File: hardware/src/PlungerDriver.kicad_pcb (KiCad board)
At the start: 2 copper layers, 80 x 16 mm, 35 parts, among them J1 MC 1,5/2, J2 locked, J3 S2B-PH, U1 16F1454, U2 TB67H450AFNG

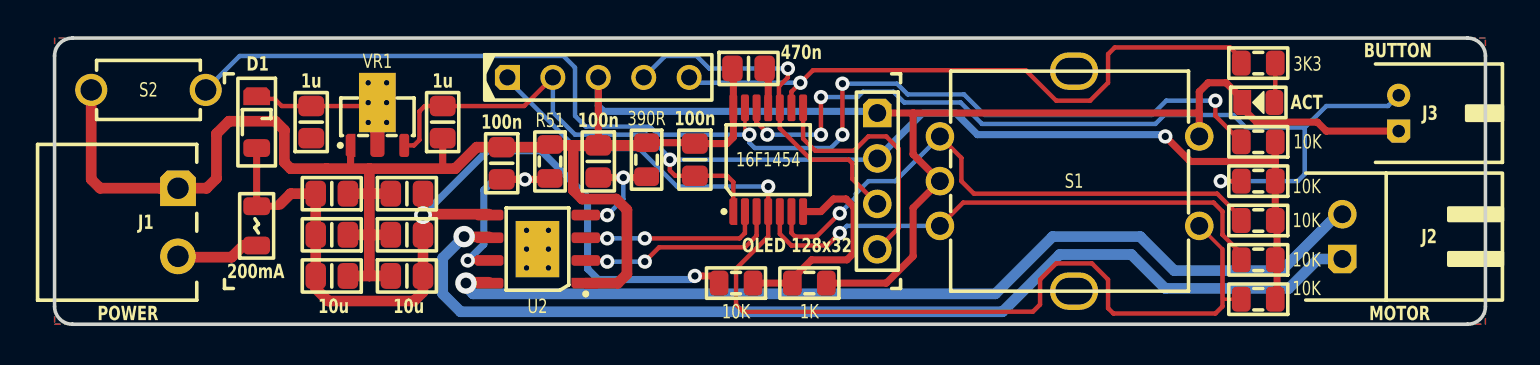
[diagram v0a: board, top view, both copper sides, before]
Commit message: Swapped I2C/SPI lines + general footprint update
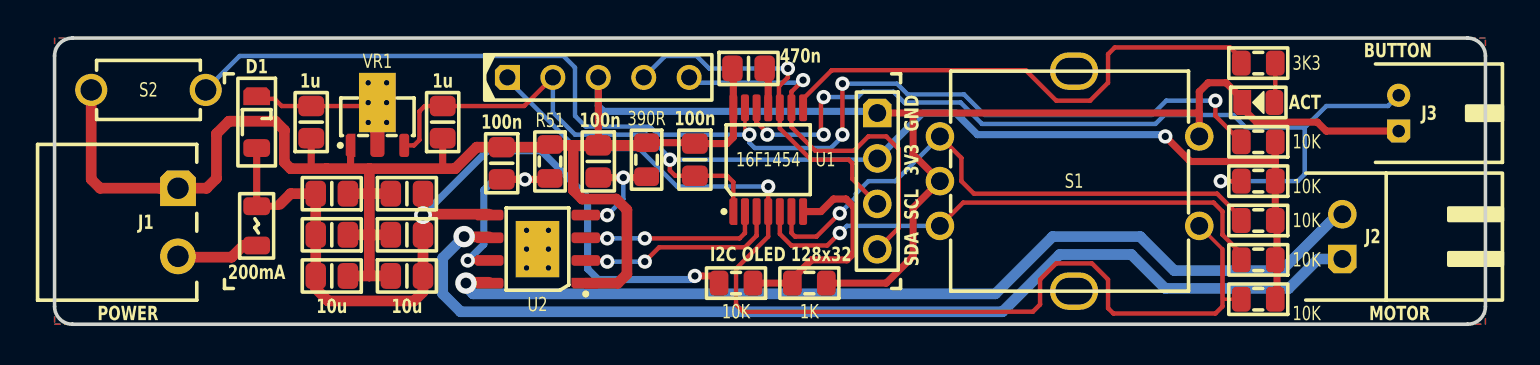
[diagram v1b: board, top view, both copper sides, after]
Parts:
- DS2: value OLED 128x32 -> I2C OLED 128x32
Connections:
- net OLED_SCK renamed OLED_SCL
- C5 pad 1: (no net) -> GND
- DS2 pad 4: OLED_SDO -> OLED_SDA
- ICSP pad 5: LED_ACT -> OLED_SDA
- U1 pad 8: OLED_SDO -> LED_ACT
- U1 pad 9: LED_ACT -> OLED_SDA
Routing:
- net OLED_SDA: track 0.00 -> 22.3 mm, vias 0 -> 1
- net OLED_SDO: track 14.1 -> 0.00 mm
- net LED_ACT: track 35.6 -> 28.8 mm, vias 1 -> 0
- net GND: track 153.6 -> 157.5 mm
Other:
- board text added: "3V3"
- board text added: "GND"
- board text added: "SCL"
- board text added: "SDA"

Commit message: Refactoring board a bit more
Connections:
- net Vdio renamed 5V
- net Vfused renamed 6V

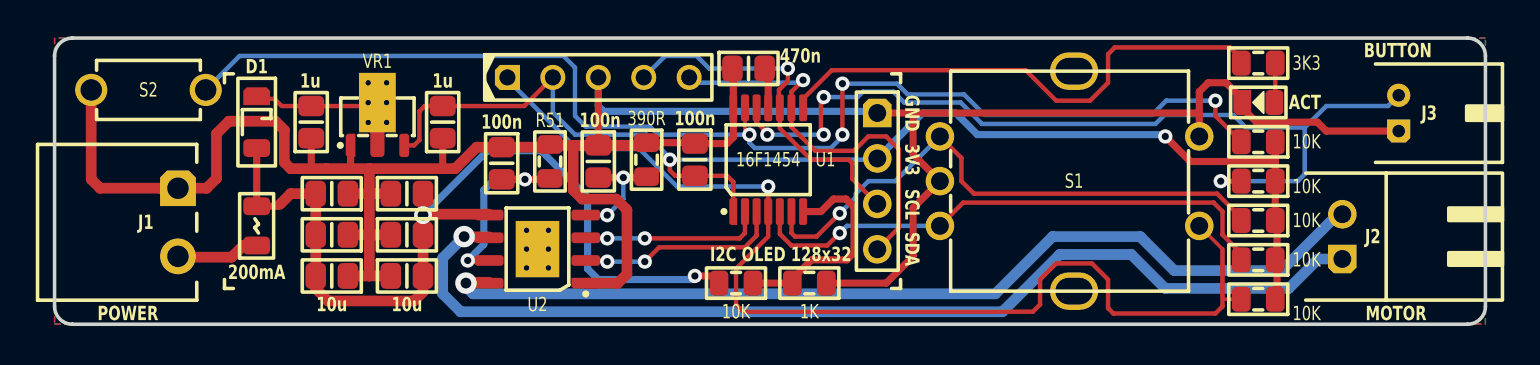
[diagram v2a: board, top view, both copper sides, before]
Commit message: Added I2C pullup resistors
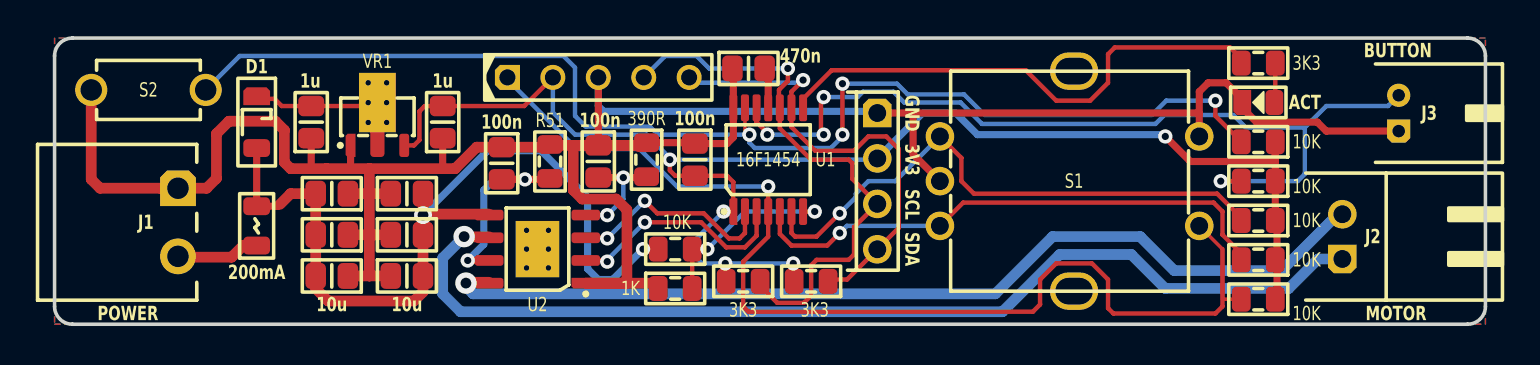
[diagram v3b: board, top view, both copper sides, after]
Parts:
- added R5: 3K3, Medo64:R (0805), F.Cu at (53.5, 28.6)
- added R6: 3K3, Medo64:R (0805), F.Cu at (57.3, 28.6)
- moved R3 7.51 mm to (49.7, 29.0), turned to 0 degrees
- moved R12 3.89 mm to (49.7, 26.8)
- renumbered R9 to R10, R10 to R11, R5 to R12, R6 to R7, R7 to R8, R8 to R9
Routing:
- net 3V3: track 72.2 -> 83.7 mm, vias 2 -> 5
- net OLED_SCL: track 20.0 -> 31.4 mm
- net GND: track 157.5 -> 151.7 mm
- net OLED_SDA: track 22.3 -> 25.8 mm
- net 6V: track 51.3 -> 48.6 mm
- net IN_ADC_INPUT_VOLTAGE: track 12.1 -> 10.4 mm, vias 0 -> 2
- net DRIVER_IN1: track 10.3 -> 12.0 mm
- net DRIVER_IN2: track 11.4 -> 12.7 mm
- net IN_ROTARY_SWITCH: track 65.0 -> 64.5 mm

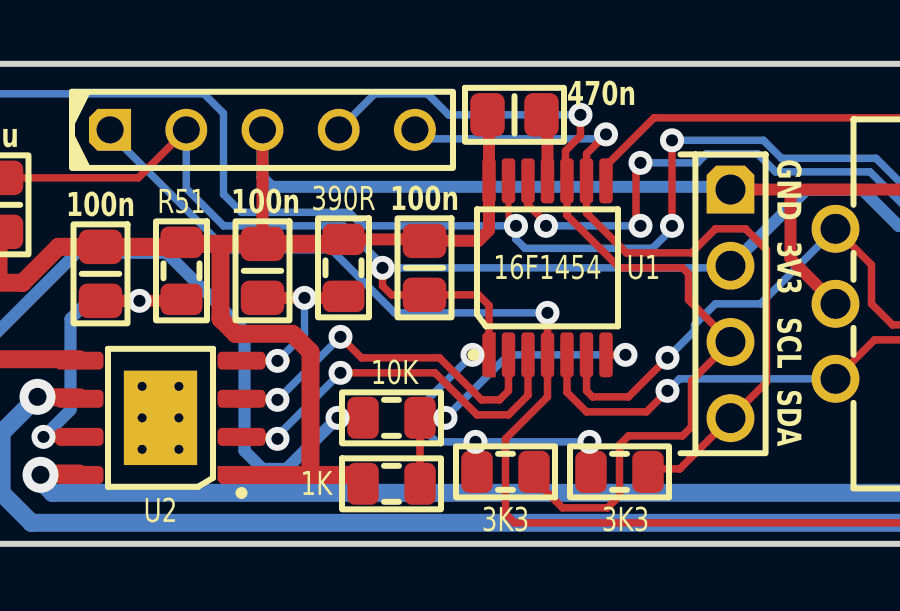
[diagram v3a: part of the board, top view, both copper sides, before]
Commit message: Moving resistors a bit
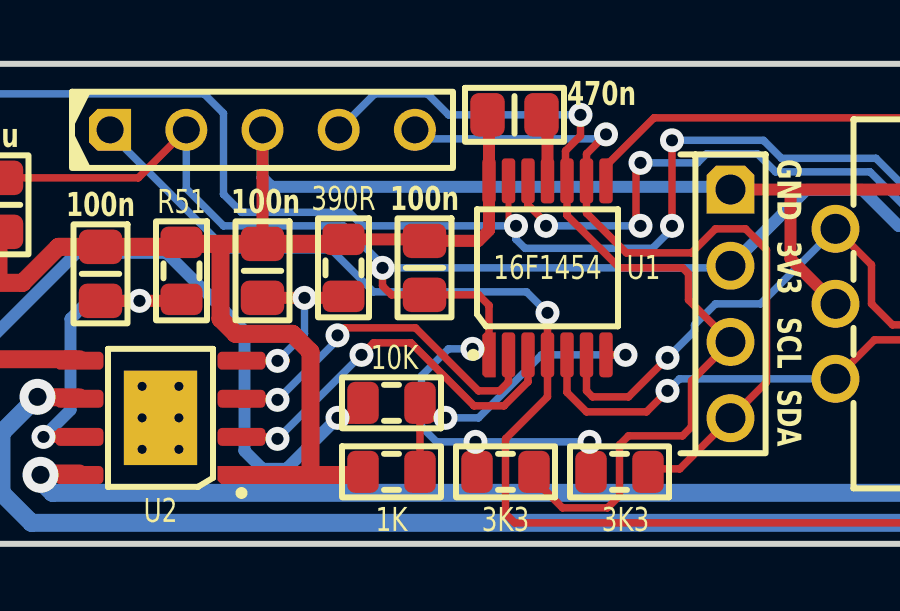
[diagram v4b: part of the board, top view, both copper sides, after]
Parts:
- moved R12 0.50 mm to (49.7, 26.3)
- moved R3 0.40 mm to (49.7, 28.6)
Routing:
- net 3V3: track 83.7 -> 84.3 mm
- net LED_ACT: track 28.8 -> 28.3 mm

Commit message: Refacored I2C pull up resistors
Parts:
- R11: renamed from R5; value 3K3 -> 5K1; footprint Medo64:R (0805) -> Medo64:R Optional (0805)
- R12: renamed from R6; value 3K3 -> 5K1; footprint Medo64:R (0805) -> Medo64:R Optional (0805)
- renumbered R12 to R10, R7 to R5, R8 to R6, R9 to R7, R10 to R8, R11 to R9
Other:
- board text added: "PULL-UP"
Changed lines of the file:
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@@
     )
   )
-  (footprint "Medo64:R (0805)" (layer "F.Cu")
+  (footprint "Medo64:R Optional (0805)" (layer "F.Cu")
     (at 53.5 28.6 180)
-    (descr "RESC2013X70N")
-    (attr smd)
-    (fp_text reference "R5" (at 0 -1.6) (layer "F.SilkS") hide
-        (effects (font (size 0.8 0.6) (thickness 0.15)))
-    )
-    (fp_text value "3K3" (at 0 -1.6) (layer "F.SilkS")
+    (tags "RESC2013X70N")
+    (attr smd exclude_from_bom)
+    (fp_text reference "R11" (at 0 -1.6 180) (layer "F.SilkS") hide
+        (effects (font (size 0.8 0.6) (thickness 0.15)))
+    )
+    (fp_text value "5K1" (at 0 1.7 180) (layer "F.SilkS") hide
         (effects (font (size 0.8 0.6) (thickness 0.15)))
     )
@@
       (stroke (width 0.2) (type default)) (layer "F.SilkS"))
     (fp_rect (start -1.65 -0.85) (end 1.65 0.85)
-      (stroke (width 0.2) (type default)) (fill none) (layer "F.SilkS"))
+      (stroke (width 0.2) (type dash)) (fill none) (layer "F.SilkS"))
     (fp_rect (start -1.75 -0.95) (end 1.75 0.95)
       (stroke (width 0.01) (type dash)) (fill none) (layer "F.CrtYd"))
     (fp_rect (start -1 -0.625) (end 1 0.625)
       (stroke (width 0.01) (type dash_dot)) (fill none) (layer "F.Fab"))
-    (pad "1" smd roundrect (at -0.95 0 180) (size 1.05 1.4) (layers "F.Cu" "F.Paste" "F.Mask") (roundrect_rratio 0.25)
+    (pad "1" smd roundrect (at -0.95 0 180) (size 1.05 1.4) (layers "F.Cu" "F.Mask") (roundrect_rratio 0.25)
       (net 19 "OLED_SCL") (thermal_bridge_angle 45))
-    (pad "2" smd roundrect (at 0.95 0 180) (size 1.05 1.4) (layers "F.Cu" "F.Paste" "F.Mask") (roundrect_rratio 0.25)
+    (pad "2" smd roundrect (at 0.95 0 180) (size 1.05 1.4) (layers "F.Cu" "F.Mask") (roundrect_rratio 0.25)
       (net 4 "3V3") (thermal_bridge_angle 45))
-    (model ":KICAD7_3DMODEL_DIR:Resistor_SMD.3dshapes/R_0805_2012Metric.step"
-      (offset (xyz 0 0 0))
-      (scale (xyz 1 1 1))
-      (rotate (xyz 0 0 0))
-    )
   )
   (footprint "Medo64:C (0805)" (layer "F.Cu")
@@
   (footprint "Medo64:R (0805)" (layer "F.Cu")
     (at 82.3 29.6 180)
-    (descr "RESC2013X70N")
-    (attr smd)
-    (fp_text reference "R11" (at 0 -1.6 180) (layer "F.SilkS") hide
+    (tags "RESC2013X70N")
+    (attr smd)
+    (fp_text reference "R9" (at 0 -1.6 180) (layer "F.SilkS") hide
         (effects (font (size 0.8 0.6) (thickness 0.15)))
     )
@@
   (footprint "Medo64:R (0805)" (layer "F.Cu")
     (at 82.3 23 180)
-    (descr "RESC2013X70N")
-    (attr smd)
-    (fp_text reference "R8" (at 0 -1.6 180) (layer "F.SilkS") hide
+    (tags "RESC2013X70N")
+    (attr smd)
+    (fp_text reference "R6" (at 0 -1.6 180) (layer "F.SilkS") hide
         (effects (font (size 0.8 0.6) (thickness 0.15)))
     )
@@
   (footprint "Medo64:R (0805)" (layer "F.Cu")
     (at 82.3 20.8 180)
-    (descr "RESC2013X70N")
-    (attr smd)
-    (fp_text reference "R7" (at 0 -1.6 180) (layer "F.SilkS") hide
+    (tags "RESC2013X70N")
+    (attr smd)
+    (fp_text reference "R5" (at 0 -1.6 180) (layer "F.SilkS") hide
         (effects (font (size 0.8 0.6) (thickness 0.15)))
     )
@@
   (footprint "Medo64:R (0805)" (layer "F.Cu")
     (at 49.7 28.6)
-    (descr "RESC2013X70N")
+    (tags "RESC2013X70N")
     (attr smd)
     (fp_text reference "R3" (at 0 -1.6) (layer "F.SilkS") hide
@@
     )
   )
-  (footprint "Medo64:R (0805)" (layer "F.Cu")
+  (footprint "Medo64:R Optional (0805)" (layer "F.Cu")
     (at 57.3 28.6 180)
-    (descr "RESC2013X70N")
-    (attr smd)
-    (fp_text reference "R6" (at 0 -1.6) (layer "F.SilkS") hide
-        (effects (font (size 0.8 0.6) (thickness 0.15)))
-    )
-    (fp_text value "3K3" (at -0.2 -1.6) (layer "F.SilkS")
+    (tags "RESC2013X70N")
+    (attr smd exclude_from_bom)
+    (fp_text reference "R12" (at 0 -1.6 180) (layer "F.SilkS") hide
+        (effects (font (size 0.8 0.6) (thickness 0.15)))
+    )
+    (fp_text value "5K1" (at 0 1.7 180) (layer "F.SilkS") hide
         (effects (font (size 0.8 0.6) (thickness 0.15)))
     )
@@
       (stroke (width 0.2) (type default)) (layer "F.SilkS"))
     (fp_rect (start -1.65 -0.85) (end 1.65 0.85)
-      (stroke (width 0.2) (type default)) (fill none) (layer "F.SilkS"))
+      (stroke (width 0.2) (type dash)) (fill none) (layer "F.SilkS"))
     (fp_rect (start -1.75 -0.95) (end 1.75 0.95)
       (stroke (width 0.01) (type dash)) (fill none) (layer "F.CrtYd"))
     (fp_rect (start -1 -0.625) (end 1 0.625)
       (stroke (width 0.01) (type dash_dot)) (fill none) (layer "F.Fab"))
-    (pad "1" smd roundrect (at -0.95 0 180) (size 1.05 1.4) (layers "F.Cu" "F.Paste" "F.Mask") (roundrect_rratio 0.25)
+    (pad "1" smd roundrect (at -0.95 0 180) (size 1.05 1.4) (layers "F.Cu" "F.Mask") (roundrect_rratio 0.25)
       (net 20 "OLED_SDA") (thermal_bridge_angle 45))
-    (pad "2" smd roundrect (at 0.95 0 180) (size 1.05 1.4) (layers "F.Cu" "F.Paste" "F.Mask") (roundrect_rratio 0.25)
+    (pad "2" smd roundrect (at 0.95 0 180) (size 1.05 1.4) (layers "F.Cu" "F.Mask") (roundrect_rratio 0.25)
       (net 4 "3V3") (thermal_bridge_angle 45))
-    (model ":KICAD7_3DMODEL_DIR:Resistor_SMD.3dshapes/R_0805_2012Metric.step"
-      (offset (xyz 0 0 0))
-      (scale (xyz 1 1 1))
-      (rotate (xyz 0 0 0))
-    )
   )
   (footprint "Medo64:R (0805)" (layer "F.Cu")
     (at 48.1 21.8 -90)
-    (descr "RESC2013X70N")
+    (tags "RESC2013X70N")
     (attr smd)
     (fp_text reference "R2" (at 0 -1.6 -90) (layer "F.SilkS") hide
@@
   (footprint "Medo64:R (0805)" (layer "F.Cu")
     (at 82.3 16.4)
-    (descr "RESC2013X70N")
+    (tags "RESC2013X70N")
     (attr smd)
     (fp_text reference "R4" (at 0 -1.6) (layer "F.SilkS") hide
@@
   (footprint "Medo64:R (0805)" (layer "F.Cu")
     (at 82.3 25.2 180)
-    (descr "RESC2013X70N")
-    (attr smd)
-    (fp_text reference "R9" (at 0 -1.6 180) (layer "F.SilkS") hide
+    (tags "RESC2013X70N")
+    (attr smd)
+    (fp_text reference "R7" (at 0 -1.6 180) (layer "F.SilkS") hide
         (effects (font (size 0.8 0.6) (thickness 0.15)))
     )
@@
   (footprint "Medo64:R (0805)" (layer "F.Cu")
     (at 49.7 26.3 180)
-    (descr "RESC2013X70N")
-    (attr smd)
-    (fp_text reference "R12" (at 0 -1.6) (layer "F.SilkS") hide
+    (tags "RESC2013X70N")
+    (attr smd)
+    (fp_text reference "R10" (at 0 -1.6) (layer "F.SilkS") hide
         (effects (font (size 0.8 0.6) (thickness 0.15)))
     )
@@
   (footprint "Medo64:R (0805)" (layer "F.Cu")
     (at 82.3 27.4 180)
-    (descr "RESC2013X70N")
-    (attr smd)
-    (fp_text reference "R10" (at 0 -1.6 180) (layer "F.SilkS") hide
+    (tags "RESC2013X70N")
+    (attr smd)
+    (fp_text reference "R8" (at 0 -1.6 180) (layer "F.SilkS") hide
         (effects (font (size 0.8 0.6) (thickness 0.15)))
     )
@@
   (footprint "Medo64:R (0805)" (layer "F.Cu")
     (at 42.7 21.9 -90)
-    (descr "RESC2013X70N")
+    (tags "RESC2013X70N")
     (attr smd)
     (fp_text reference "R1" (at 0 -1.6 -90) (layer "F.SilkS") hide
@@
     (effects (font (size 0.8 0.6) (thickness 0.15) bold))
   )
+  (gr_text "PULL-UP" (at 55.4 29.7) (layer "F.SilkS")
+    (effects (font (size 0.8 0.6) (thickness 0.15) bold) (justify top))
+  )
   (gr_text "GND" (at 63.4 19.2 270) (layer "F.SilkS")

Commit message: Added icon and title
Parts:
- added ICON: Medo64, Medo64:ICON Medo64, B.Cu at (92.0, 26.7)
- DS2: footprint Medo64:DS OLED 128x32 SPI (4w) -> Medo64:DS OLED 128x32 I2C (4w)
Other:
- board text added: "PlungerDriver A"

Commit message: Increased LED resistor value
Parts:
- R4: value 3K3 -> 10K
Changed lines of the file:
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@@
         (effects (font (size 0.8 0.6) (thickness 0.15)))
     )
-    (fp_text value "3K3" (at 2.7 0) (layer "F.SilkS")
+    (fp_text value "10K" (at 2.7 0) (layer "F.SilkS")
         (effects (font (size 0.8 0.6) (thickness 0.15)))
     )

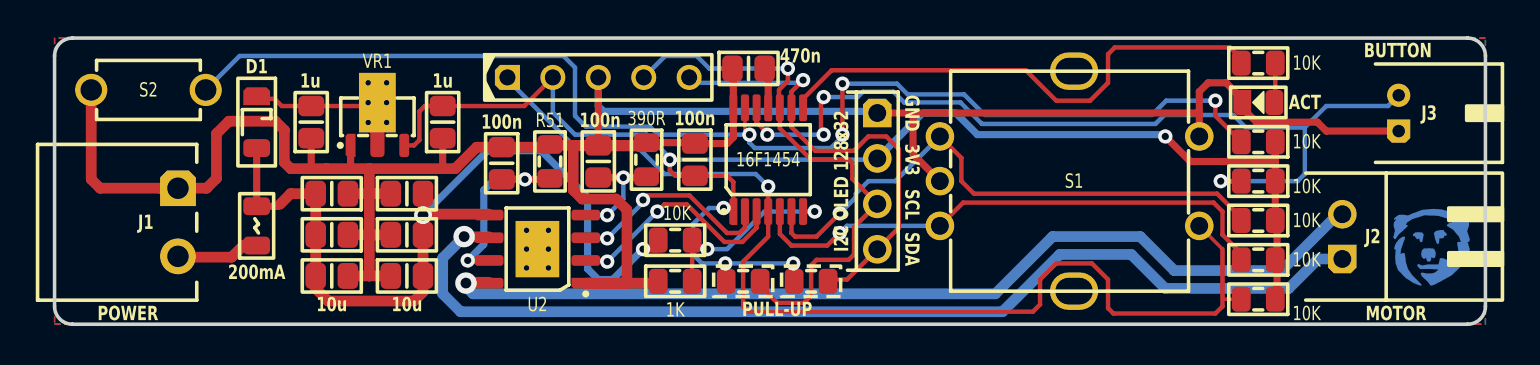
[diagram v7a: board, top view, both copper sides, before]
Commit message: Fixed missing Vref divider resistor (doh!)
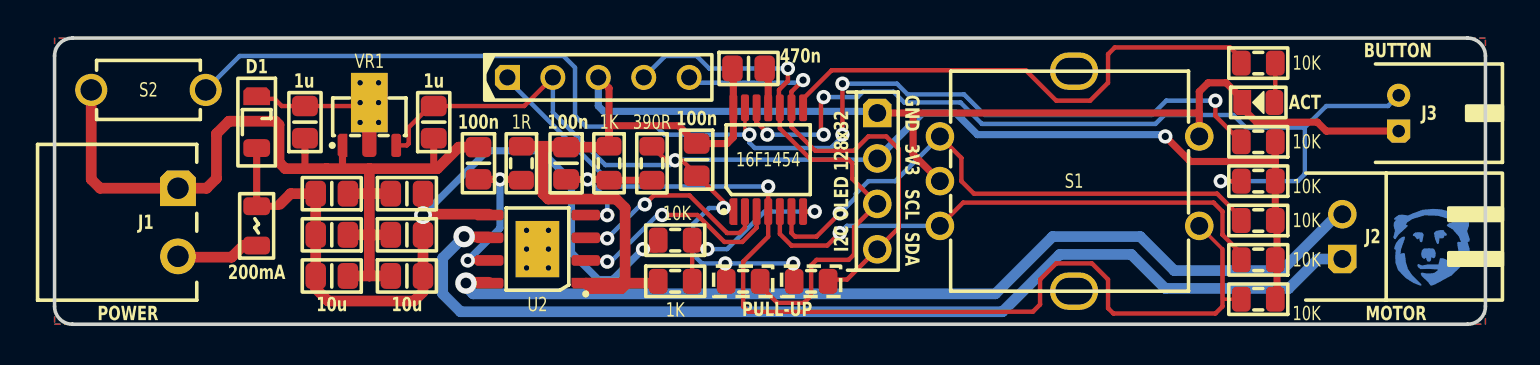
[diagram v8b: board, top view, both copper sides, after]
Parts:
- added R2: 390R, Medo64:R (0805), F.Cu at (48.4, 22.0)
- R1: value R51 -> 1R
- R3: renamed from R2; value 390R -> 1K
- moved R3 2.11 mm to (46.0, 22.0)
- moved C2 1.80 mm to (43.6, 22.0)
- moved R1 1.60 mm to (41.1, 22.0)
- moved C3 1.30 mm to (38.7, 22.0)
- moved C6 0.50 mm to (36.2, 19.7)
- moved VR1 0.45 mm to (32.6, 21.0)
- moved C5 0.35 mm to (29.0, 19.7)
- moved C1 0.10 mm to (50.9, 21.8)
- renumbered R9 to R10, R10 to R11, R11 to R12, R12 to R13, R3 to R4, R4 to R5, R5 to R6, R6 to R7, R7 to R8, R8 to R9
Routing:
- net GND: track 151.7 -> 154.1 mm
- net DRIVER_VREF: track 6.42 -> 8.80 mm
- net DRIVER_RS: track 12.1 -> 10.3 mm
